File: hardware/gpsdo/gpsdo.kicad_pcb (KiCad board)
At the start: 4 copper layers, 70 x 70 mm, 88 parts, among them J1 Conn_01x02, J2 Conn_02x03_Top_Bottom, J3 USB_C_Receptacle_USB2.0_14P, J4 Conn_01x03, J5 Conn_Coaxial, U1 74HC4040D_652, U2 74HC4040D_652, U3 REF5040AD, U4 AD5541A, U5 OPA197xD, U6 STM32F411CEUx, U7 AMS1117-3.3, U9 SN74LVC1G125DBV, X1 X322516MLB4SI

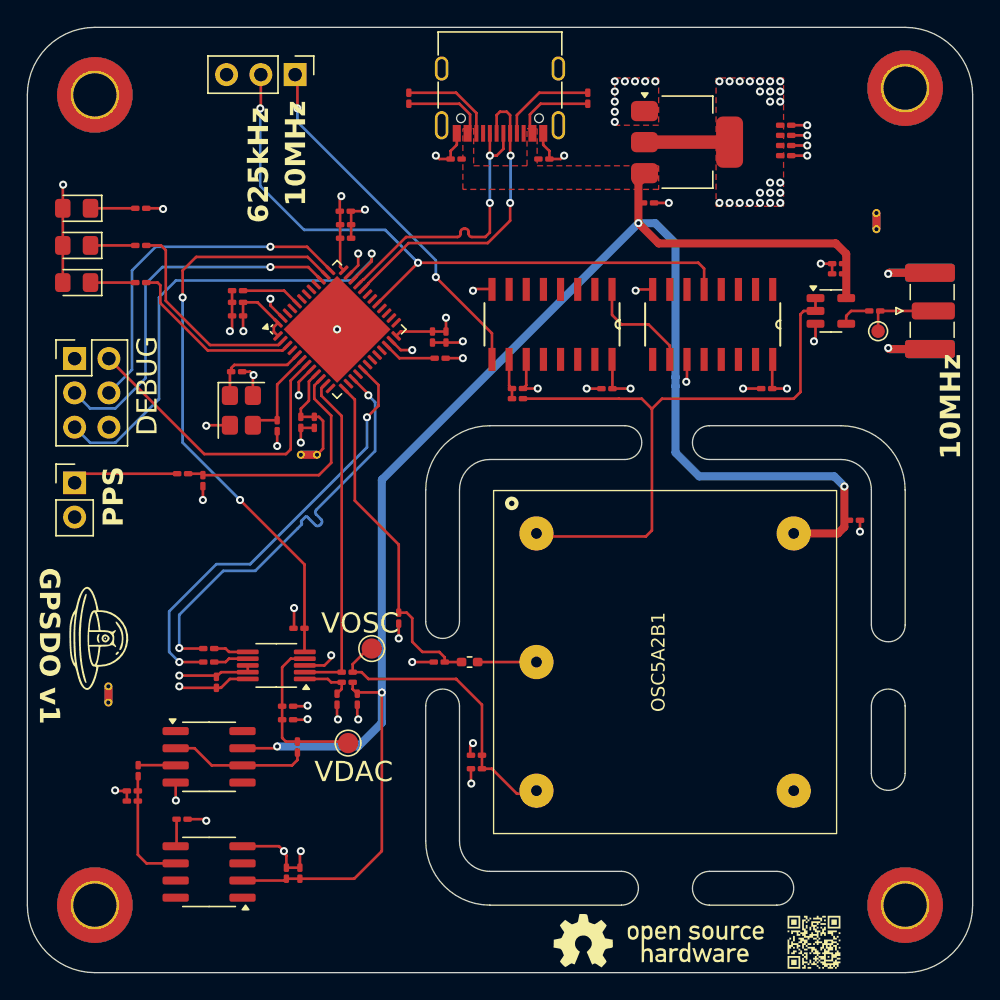
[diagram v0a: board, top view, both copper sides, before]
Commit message: update routing; bugfix in downsampling; replace voltage dividers with level shifter
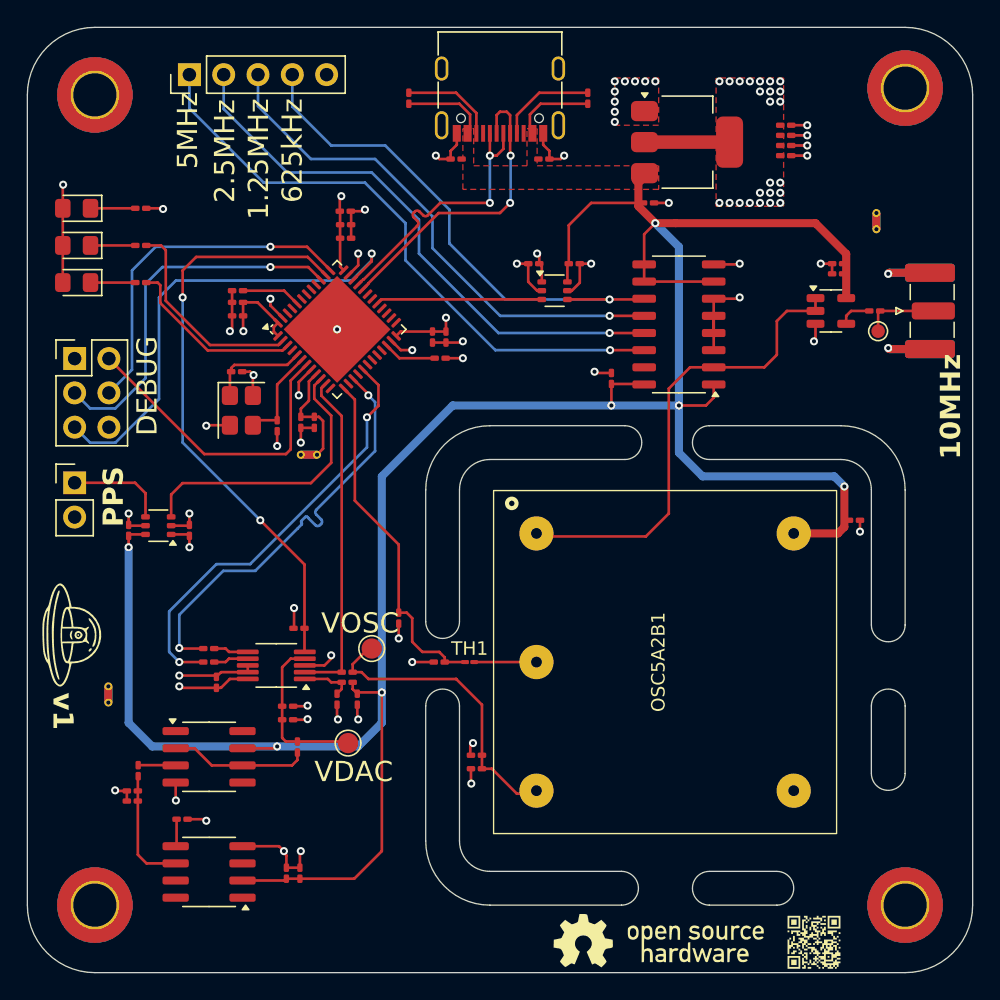
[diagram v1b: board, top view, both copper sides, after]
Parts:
- removed J4: Conn_01x03, Connector_PinHeader_2.54mm:PinHeader_1x03_P2.54mm_Vertical
- removed R10, R2: 1.1k, Resistor_SMD:R_0201_0603Metric_Pad0.64x0.40mm_HandSolder
- removed R11, R3: 2.2k, Resistor_SMD:R_0201_0603Metric_Pad0.64x0.40mm_HandSolder
- added C38: 100n, Capacitor_SMD:C_0201_0603Metric_Pad0.64x0.40mm_HandSolder, F.Cu at (148.2, 82.2)
- added C39: 100n, Capacitor_SMD:C_0201_0603Metric_Pad0.64x0.40mm_HandSolder, F.Cu at (145.2, 82.2)
- added C40: 100n, Capacitor_SMD:C_0201_0603Metric_Pad0.64x0.40mm_HandSolder, F.Cu at (119.8, 102.0)
- added J7: Conn_01x05, Connector_PinHeader_2.54mm:PinHeader_1x05_P2.54mm_Vertical, F.Cu at (119.8, 68.2)
- added U8: 74HC161, Package_SO:SO-16_3.9x9.9mm_P1.27mm, F.Cu at (156.0, 86.8)
- TH1: footprint Resistor_SMD:R_0402_1005Metric_Pad0.72x0.64mm_HandSolder -> Capacitor_SMD:C_01005_0402Metric_Pad0.57x0.30mm_HandSolder
- U1, U2: value 74HC4040D_652 -> SN74LVC1T45DCK; footprint nexperia:SOIC127P600X175-16N -> Package_TO_SOT_SMD:SOT-363_SC-70-6
- moved U2 43.7 mm to (117.5, 101.7), turned to 180 degrees
- moved C2 36.9 mm to (115.2, 102.0), turned to 90 degrees
- moved C1 11.5 mm to (151.0, 90.8), turned to 90 degrees
- moved U1 2.50 mm to (146.8, 84.2), turned to 0 degrees
- moved G*** 2.02 mm to (111.0, 109.8)
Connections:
- C1 pad 1: VDD_3V3 -> VCC_5V
- C2 pad 1: VDD_3V3 -> VCC_5V
- U1 pad 1: CNT_Q11 -> VDD_3V3
- U1 pad 2: unconnected-(U1-Q5-Pad2) -> GND
- U1 pad 3: unconnected-(U1-Q4-Pad3) -> OCXO_625KHZ_3V3
- U1 pad 4: unconnected-(U1-Q6-Pad4) -> OCXO_625KHZ
- U1 pad 5: unconnected-(U1-Q3-Pad5) -> GND
- U1 pad 6: unconnected-(U1-Q2-Pad6) -> VCC_5V
- U2 pad 1: unconnected-(U2-Q11-Pad1) -> VDD_3V3
- U2 pad 2: unconnected-(U2-Q5-Pad2) -> GND
- U2 pad 3: unconnected-(U2-Q4-Pad3) -> PPS_3V3
- U2 pad 4: unconnected-(U2-Q6-Pad4) -> PPS_5V
- U2 pad 5: OCXO_625KHZ -> GND
- U2 pad 6: unconnected-(U2-Q2-Pad6) -> VCC_5V
- U6 pad 29: OCXO_625KHZ -> OCXO_625KHZ_3V3
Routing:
- net VCC_5V: track 156.7 -> 206.8 mm, vias 4 -> 7
- net OCXO_5MHZ: track 0.00 -> 45.2 mm, vias 0 -> 1
- net OCXO_2.5MHZ: track 0.00 -> 42.0 mm, vias 0 -> 1
- net OCXO_1.25MHZ: track 0.00 -> 38.7 mm, vias 0 -> 1
- net OCXO_10MHZ: track 26.9 -> 0.00 mm, vias 2 -> 0
- net OCXO_625KHZ_3V3: track 0.00 -> 12.3 mm
- net OCXO_Out: track 47.0 -> 35.4 mm
- net OCXO_625KHZ: track 49.5 -> 39.0 mm, vias 2 -> 1
- net GND: track 55.2 -> 65.3 mm
- net CNT_Q11: track 8.38 -> 0.00 mm
- net PPS_3V3: track 18.0 -> 21.4 mm
- net Net-(U1-~CP): track 2.98 -> 0.00 mm
- net VDD_3V3: track 45.7 -> 43.5 mm
- net GNDA: track 41.2 -> 42.0 mm
- net USB_N: track 23.5 -> 22.7 mm
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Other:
- board text added: "1.25MHz"
- board text added: "2.5MHz"
- board text added: "5MHz"
- board text added: "v1"
- board text removed: "${REFERENCE}"
- board text removed: "GPSDO v1"

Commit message: update layout
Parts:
- moved NT1 18.7 mm to (129.5, 104.8)
- moved NT3 6.63 mm to (164.5, 82.2), turned to 180 degrees
- moved C32 3.76 mm to (135.0, 104.8), turned to 180 degrees
- moved R7 0.92 mm to (128.8, 109.5), turned to 0 degrees
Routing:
- net AD5541A_CS: track 43.5 -> 44.8 mm

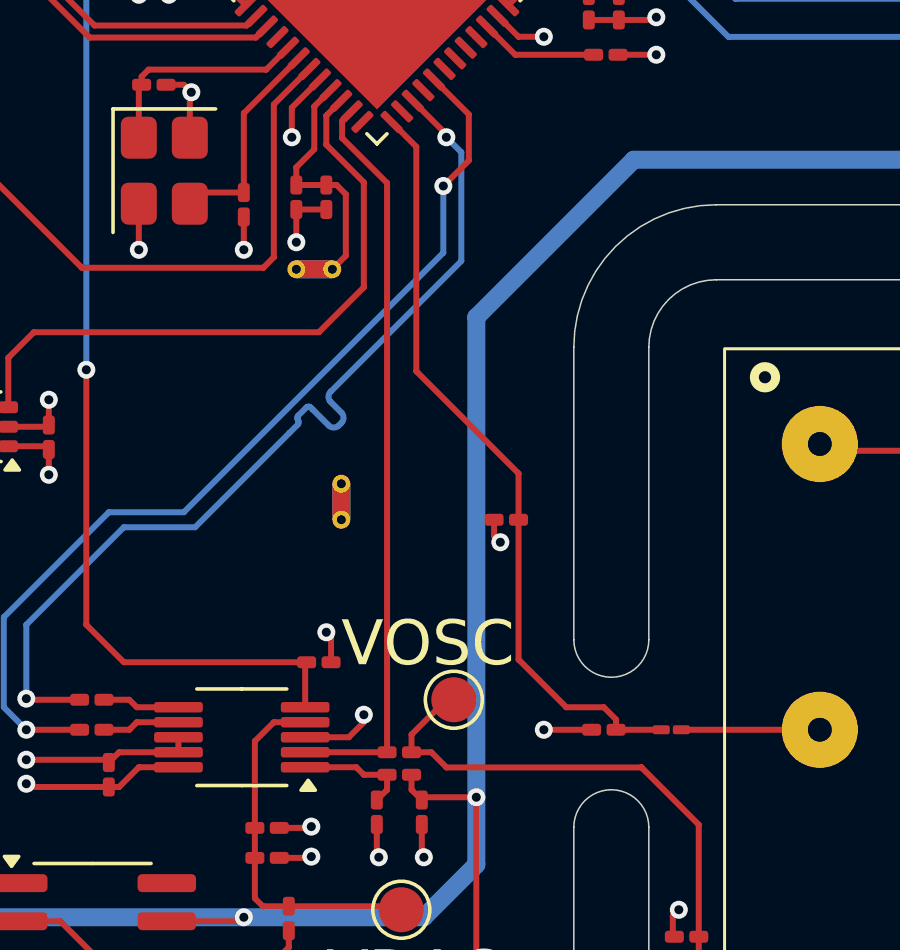
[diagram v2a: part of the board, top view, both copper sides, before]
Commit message: version 1 put into production
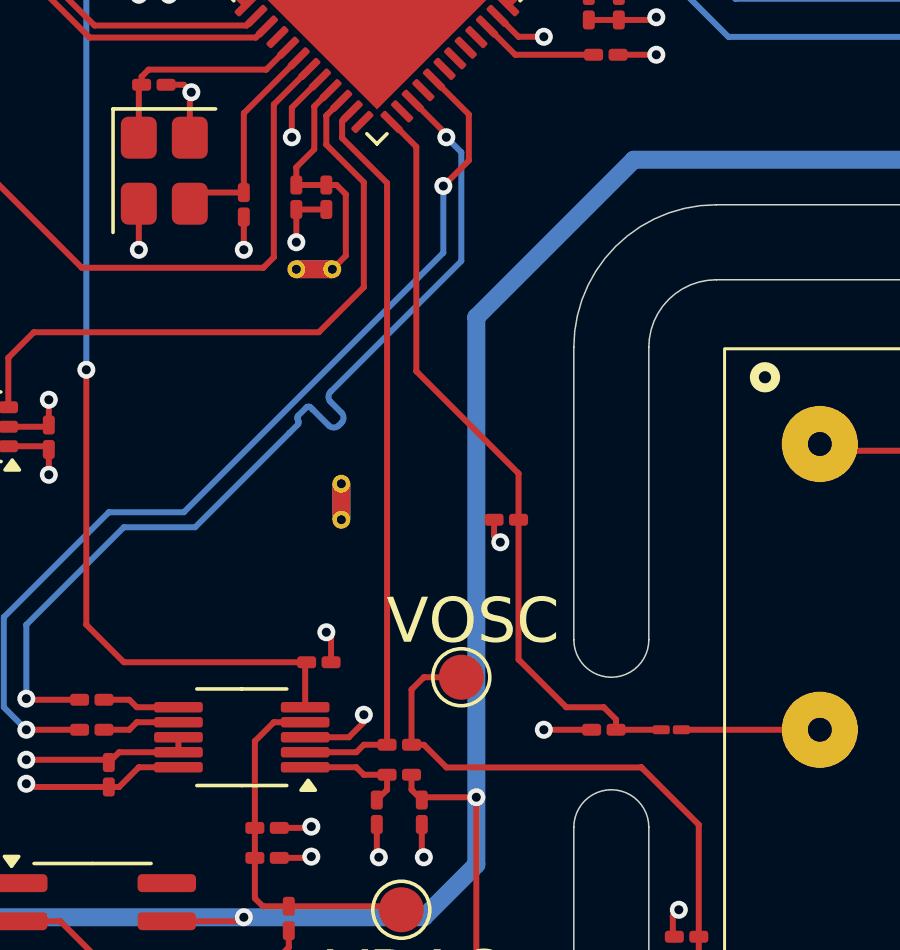
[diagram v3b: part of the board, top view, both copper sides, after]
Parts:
- L1: value 10u -> 10uH
- moved TP1 0.79 mm to (133.5, 110.0)
- moved R1 0.25 mm to (131.4, 112.2)
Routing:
- net Net-(OSC5A2B1-Vref): track 22.3 -> 23.9 mm

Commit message: revisit footprints
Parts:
- C1, C10, C11, C12, C13, C14, C15, C16, C17, C18, C19, C2, C20, C21, C22, C23, C24, C25, C26, C27, C28, C29, C3, C30, C31, C32, C33, C34, C35, C36, C37, C38, C39, C4, C40, C5, C6, C7, C8, C9: footprint Capacitor_SMD:C_0201_0603Metric_Pad0.64x0.40mm_HandSolder -> Capacitor_SMD:C_0603_1608Metric
- L1: footprint Capacitor_SMD:C_0201_0603Metric_Pad0.64x0.40mm_HandSolder -> Inductor_SMD:L_0603_1608Metric
- R1, R12, R13, R14, R15, R16, R17, R18, R4, R5, R6, R7, R8, R9: footprint Resistor_SMD:R_0201_0603Metric_Pad0.64x0.40mm_HandSolder -> Resistor_SMD:R_0603_1608Metric
- TH1: footprint Capacitor_SMD:C_01005_0402Metric_Pad0.57x0.30mm_HandSolder -> Resistor_SMD:R_0603_1608Metric
- moved C35 11.4 mm to (150.5, 77.5), turned to -90 degrees
- moved NT3 6.83 mm to (170.9, 79.8), turned to 90 degrees
- moved C17 4.23 mm to (122.3, 95.9), turned to 180 degrees
- moved C34 4.07 mm to (148.8, 77.5), turned to -90 degrees
- moved C4 2.60 mm to (141.0, 122.2), turned to -90 degrees
- moved R7 2.55 mm to (126.2, 109.0), turned to 180 degrees
- moved TP3 2.26 mm to (131.2, 120.0)
- moved C27 2.15 mm to (126.2, 95.2)
- moved C26 1.77 mm to (127.8, 95.2)
- moved C5 1.75 mm to (169.0, 103.0), turned to -90 degrees
- moved TP1 1.60 mm to (132.2, 109.0)
- moved R17 1.52 mm to (136.8, 111.5)
- moved C18 1.51 mm to (138.5, 90.8)
- moved C7 1.29 mm to (132.5, 115.8)
- moved X1 1.27 mm to (122.3, 92.9)
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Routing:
- net GND: track 65.1 -> 77.4 mm, vias 38 -> 35
- net GNDA: track 41.7 -> 47.6 mm, vias 18 -> 16
- net VDD_3V3: track 43.1 -> 48.8 mm, vias 33 -> 29
- net NRST: track 23.3 -> 26.7 mm
- net OSC_IN: track 7.23 -> 10.1 mm
- net DAC_Vref: track 11.6 -> 13.7 mm
- net OSC_OUT: track 6.66 -> 8.37 mm
- net AD5541A_SCLK: track 31.8 -> 30.5 mm
- net AD5541A_DIN: track 31.9 -> 30.6 mm
- net AD5541A_CS: track 44.8 -> 46.0 mm
- net VDDA_3V3: track 8.10 -> 9.30 mm
- net OCXO_Temperature: track 25.3 -> 24.3 mm
- net PPS_5V: track 7.32 -> 8.39 mm
- net Net-(OSC5A2B1-Vref): track 23.9 -> 24.9 mm
- net OCXO_Vref: track 24.7 -> 23.7 mm
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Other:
- board text added: "v2"
- board text removed: "v1"
